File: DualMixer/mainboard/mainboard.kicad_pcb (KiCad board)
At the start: 2 copper layers, 35.6 x 107.9 mm, 62 parts, among them J1 IN_A1, J10 IN_B4, J11 OUTB, J12 Conn_02x05_Odd_Even, J13 Conn_01x03_Male, J2 IN_A2, J3 IN_A3, J4 OUTA, J5 Conn_02x06_Odd_Even, J6 IN_A4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

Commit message: Add missing output connectors to IO board
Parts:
- J5: value Conn_02x06_Odd_Even -> Conn_02x07_Odd_Even; footprint Connector_PinHeader_2.54mm:PinHeader_2x06_P2.54mm_Vertical -> Connector_PinHeader_2.54mm:PinHeader_2x07_P2.54mm_Vertical
- moved J5 23.3 mm to (81.8, 133.4)
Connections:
- J11 pad T: Net-(J11-PadT) -> /OUT_B
- J4 pad T: Net-(J4-PadT) -> /OUT_A
- J5 pad 10: /LEDA -> /LEDB
- J5 pad 11: GND -> /OUT_A
- J5 pad 12: /LEDB -> /OUT_B
- J5 pad 9: GND -> /LEDA
- R20 pad 2: Net-(J11-PadT) -> /OUT_B
- R21 pad 2: Net-(J4-PadT) -> /OUT_A
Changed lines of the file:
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@@
   (net 11 "Net-(J2-PadT)")
   (net 12 "Net-(J3-PadT)")
-  (net 13 "Net-(J4-PadT)")
+  (net 13 "/OUT_A")
   (net 14 "unconnected-(J4-PadTN)")
   (net 15 "/IN_A2")
@@
   (net 26 "Net-(J9-PadT)")
   (net 27 "Net-(J10-PadT)")
-  (net 28 "Net-(J11-PadT)")
+  (net 28 "/OUT_B")
   (net 29 "unconnected-(J11-PadTN)")
   (net 30 "Net-(R1-Pad1)")
@@
   (net 46 "Net-(J12-Pad1)")
   (net 47 "Net-(J12-Pad10)")
+  (net 48 "unconnected-(J5-Pad14)")
   (footprint "Resistor_SMD:R_0603_1608Metric_Pad0.98x0.95mm_HandSolder" (layer "F.Cu")
     (at 156.48 89.2)
@@
       (net 8 "Net-(D3-Pad2)") (pintype "passive"))
     (pad "2" smd roundrect (at 0.9125 0) (size 0.975 0.95) (layers "F.Cu" "F.Paste" "F.Mask") (roundrect_rratio 0.25)
-      (net 28 "Net-(J11-PadT)") (pintype "passive"))
+      (net 28 "/OUT_B") (pintype "passive"))
     (model "${KICAD6_3DMODEL_DIR}/Resistor_SMD.3dshapes/R_0603_1608Metric.wrl"
       (offset (xyz 0 0 0))
@@
       (net 2 "GND") (pintype "passive"))
     (pad "T" thru_hole circle (at 0 11.4 270) (size 2.13 2.13) (drill 1.43) (layers *.Cu *.Mask)
-      (net 28 "Net-(J11-PadT)") (pintype "passive"))
+      (net 28 "/OUT_B") (pintype "passive"))
     (pad "TN" thru_hole circle (at 0 3.1 270) (size 2.13 2.13) (drill 1.42) (layers *.Cu *.Mask)
       (net 29 "unconnected-(J11-PadTN)") (pintype "passive+no_connect"))
@@
       (net 6 "Net-(D1-Pad2)") (pintype "passive"))
     (pad "2" smd roundrect (at 0.9125 0) (size 0.975 0.95) (layers "F.Cu" "F.Paste" "F.Mask") (roundrect_rratio 0.25)
-      (net 13 "Net-(J4-PadT)") (pintype "passive"))
+      (net 13 "/OUT_A") (pintype "passive"))
     (model "${KICAD6_3DMODEL_DIR}/Resistor_SMD.3dshapes/R_0603_1608Metric.wrl"
       (offset (xyz 0 0 0))
@@
       (net 2 "GND") (pintype "passive"))
     (pad "T" thru_hole circle (at 0 11.4 90) (size 2.13 2.13) (drill 1.43) (layers *.Cu *.Mask)
-      (net 13 "Net-(J4-PadT)") (pintype "passive"))
+      (net 13 "/OUT_A") (pintype "passive"))
     (pad "TN" thru_hole circle (at 0 3.1 90) (size 2.13 2.13) (drill 1.42) (layers *.Cu *.Mask)
       (net 14 "unconnected-(J4-PadTN)") (pintype "passive+no_connect"))
@@
     )
   )
-  (footprint "Connector_PinHeader_2.54mm:PinHeader_2x06_P2.54mm_Vertical" (layer "F.Cu")
-    (at 81.87 110.19 180)
-    (descr "Through hole straight pin header, 2x06, 2.54mm pitch, double rows")
-    (tags "Through hole pin header THT 2x06 2.54mm double row")
+  (footprint "Connector_PinHeader_2.54mm:PinHeader_2x07_P2.54mm_Vertical" (layer "F.Cu")
+    (at 81.84 133.44 180)
+    (descr "Through hole straight pin header, 2x07, 2.54mm pitch, double rows")
+    (tags "Through hole pin header THT 2x07 2.54mm double row")
     (property "Sheetfile" "mainboard.kicad_sch")
     (property "Sheetname" "")
     (attr through_hole)
-    (fp_text reference "J5" (at 1.27 -2.33) (layer "F.SilkS")
-      (effects (font (size 1 1) (thickness 0.15)))
-    )
-    (fp_text value "Conn_02x06_Odd_Even" (at 1.27 15.03) (layer "F.Fab")
-      (effects (font (size 1 1) (thickness 0.15)))
-    )
-    (fp_text user "${REFERENCE}" (at 1.27 6.35 90) (layer "F.Fab")
-      (effects (font (size 1 1) (thickness 0.15)))
-    )
-    (fp_line (start -1.33 14.03) (end 3.87 14.03) (layer "F.SilkS") (width 0.12))
+    (fp_text reference "J5" (at 1.35 17.49 180) (layer "F.SilkS")
+      (effects (font (size 1 1) (thickness 0.15)))
+    )
+    (fp_text value "Conn_02x07_Odd_Even" (at 1.27 17.57 180) (layer "F.Fab")
+      (effects (font (size 1 1) (thickness 0.15)))
+    )
+    (fp_text user "${REFERENCE}" (at 1.27 7.62 270) (layer "F.Fab")
+      (effects (font (size 1 1) (thickness 0.15)))
+    )
+    (fp_line (start -1.33 1.27) (end -1.33 16.57) (layer "F.SilkS") (width 0.12))
+    (fp_line (start 3.87 -1.33) (end 3.87 16.57) (layer "F.SilkS") (width 0.12))
+    (fp_line (start -1.33 -1.33) (end 0 -1.33) (layer "F.SilkS") (width 0.12))
+    (fp_line (start -1.33 1.27) (end 1.27 1.27) (layer "F.SilkS") (width 0.12))
+    (fp_line (start -1.33 16.57) (end 3.87 16.57) (layer "F.SilkS") (width 0.12))
+    (fp_line (start 1.27 1.27) (end 1.27 -1.33) (layer "F.SilkS") (width 0.12))
+    (fp_line (start -1.33 0) (end -1.33 -1.33) (layer "F.SilkS") (width 0.12))
     (fp_line (start 1.27 -1.33) (end 3.87 -1.33) (layer "F.SilkS") (width 0.12))
-    (fp_line (start -1.33 1.27) (end 1.27 1.27) (layer "F.SilkS") (width 0.12))
-    (fp_line (start -1.33 1.27) (end -1.33 14.03) (layer "F.SilkS") (width 0.12))
-    (fp_line (start -1.33 0) (end -1.33 -1.33) (layer "F.SilkS") (width 0.12))
-    (fp_line (start -1.33 -1.33) (end 0 -1.33) (layer "F.SilkS") (width 0.12))
-    (fp_line (start 3.87 -1.33) (end 3.87 14.03) (layer "F.SilkS") (width 0.12))
-    (fp_line (start 1.27 1.27) (end 1.27 -1.33) (layer "F.SilkS") (width 0.12))
-    (fp_line (start -1.8 14.5) (end 4.35 14.5) (layer "F.CrtYd") (width 0.05))
-    (fp_line (start -1.8 -1.8) (end -1.8 14.5) (layer "F.CrtYd") (width 0.05))
-    (fp_line (start 4.35 14.5) (end 4.35 -1.8) (layer "F.CrtYd") (width 0.05))
+    (fp_line (start 4.35 17.05) (end 4.35 -1.8) (layer "F.CrtYd") (width 0.05))
     (fp_line (start 4.35 -1.8) (end -1.8 -1.8) (layer "F.CrtYd") (width 0.05))
-    (fp_line (start 3.81 -1.27) (end 3.81 13.97) (layer "F.Fab") (width 0.1))
+    (fp_line (start -1.8 -1.8) (end -1.8 17.05) (layer "F.CrtYd") (width 0.05))
+    (fp_line (start -1.8 17.05) (end 4.35 17.05) (layer "F.CrtYd") (width 0.05))
     (fp_line (start -1.27 0) (end 0 -1.27) (layer "F.Fab") (width 0.1))
-    (fp_line (start -1.27 13.97) (end -1.27 0) (layer "F.Fab") (width 0.1))
-    (fp_line (start 3.81 13.97) (end -1.27 13.97) (layer "F.Fab") (width 0.1))
+    (fp_line (start -1.27 16.51) (end -1.27 0) (layer "F.Fab") (width 0.1))
+    (fp_line (start 3.81 16.51) (end -1.27 16.51) (layer "F.Fab") (width 0.1))
+    (fp_line (start 3.81 -1.27) (end 3.81 16.51) (layer "F.Fab") (width 0.1))
     (fp_line (start 0 -1.27) (end 3.81 -1.27) (layer "F.Fab") (width 0.1))
     (pad "1" thru_hole rect (at 0 0 180) (size 1.7 1.7) (drill 1) (layers *.Cu *.Mask)
@@
       (net 22 "/IN_B3") (pinfunction "Pin_8") (pintype "passive"))
     (pad "9" thru_hole oval (at 0 10.16 180) (size 1.7 1.7) (drill 1) (layers *.Cu *.Mask)
-      (net 2 "GND") (pinfunction "Pin_9") (pintype "passive"))
+      (net 7 "/LEDA") (pinfunction "Pin_9") (pintype "passive"))
     (pad "10" thru_hole oval (at 2.54 10.16 180) (size 1.7 1.7) (drill 1) (layers *.Cu *.Mask)
-      (net 7 "/LEDA") (pinfunction "Pin_10") (pintype "passive"))
+      (net 9 "/LEDB") (pinfunction "Pin_10") (pintype "passive"))
     (pad "11" thru_hole oval (at 0 12.7 180) (size 1.7 1.7) (drill 1) (layers *.Cu *.Mask)
-      (net 2 "GND") (pinfunction "Pin_11") (pintype "passive"))
+      (net 13 "/OUT_A") (pinfunction "Pin_11") (pintype "passive"))
     (pad "12" thru_hole oval (at 2.54 12.7 180) (size 1.7 1.7) (drill 1) (layers *.Cu *.Mask)
-      (net 9 "/LEDB") (pinfunction "Pin_12") (pintype "passive"))
-    (model "${KICAD6_3DMODEL_DIR}/Connector_PinHeader_2.54mm.3dshapes/PinHeader_2x06_P2.54mm_Vertical.wrl"
-      (offset (xyz 0 0 0))
-      (scale (xyz 1 1 1))
+      (net 28 "/OUT_B") (pinfunction "Pin_12") (pintype "passive"))
+    (pad "13" thru_hole oval (at 0 15.24 180) (size 1.7 1.7) (drill 1) (layers *.Cu *.Mask)
+      (net 2 "GND") (pinfunction "Pin_13") (pintype "passive"))
+    (pad "14" thru_hole oval (at 2.54 15.24 180) (size 1.7 1.7) (drill 1) (layers *.Cu *.Mask)
+      (net 48 "unconnected-(J5-Pad14)") (pinfunction "Pin_14") (pintype "passive"))
+    (model "${KICAD6_3DMODEL_DIR}/Connector_PinHeader_2.54mm.3dshapes/PinHeader_2x07_P2.54mm_Vertical.wrl"
+      (offset (xyz 0 0 0))
+      (scale (xyz 1 1 1))

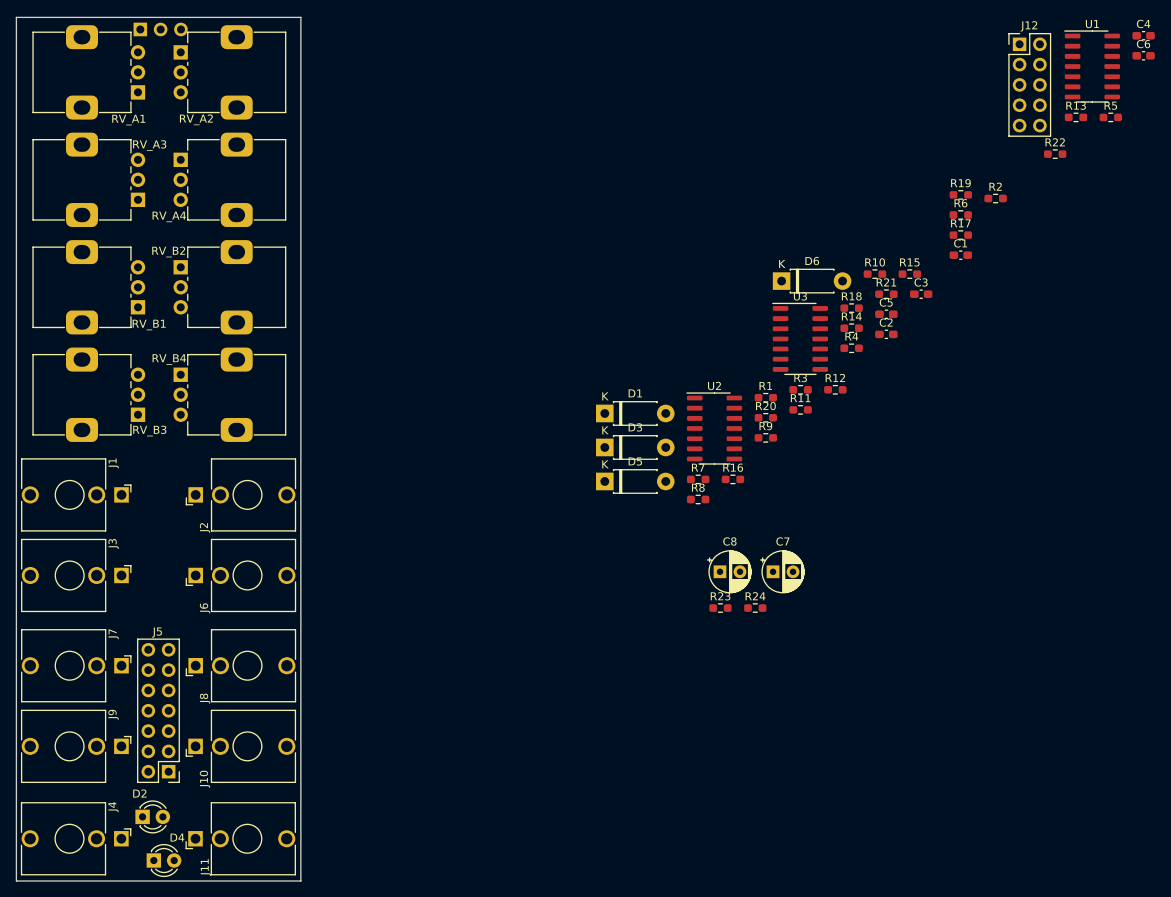
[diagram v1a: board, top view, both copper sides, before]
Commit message: Split up into mainboard and ioboard
And do routing for mainboard
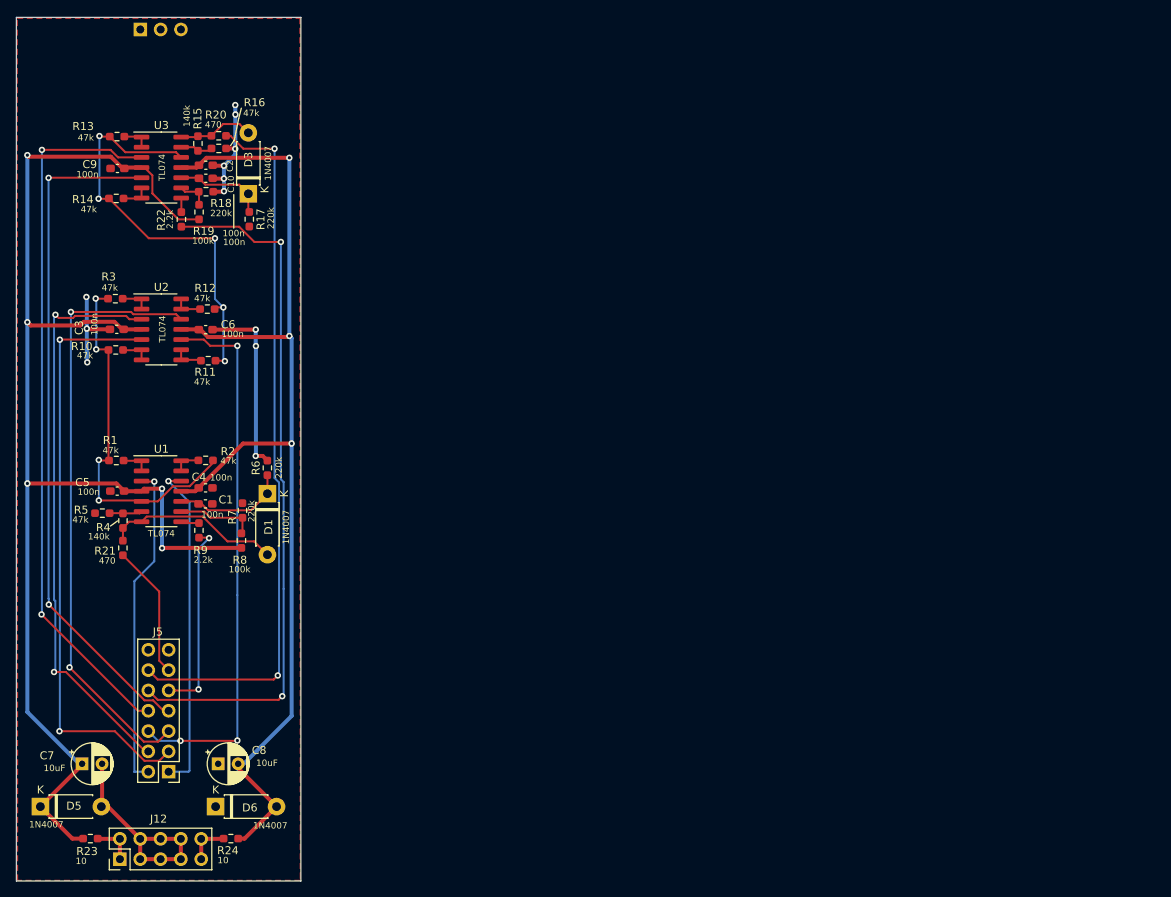
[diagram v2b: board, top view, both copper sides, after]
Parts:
- removed D2: PEAKA, LED_THT:LED_D3.0mm
- removed D4: PEAKB, LED_THT:LED_D3.0mm
- removed J1: IN_A1, Connector_Audio:Jack_3.5mm_QingPu_WQP-PJ398SM_Vertical_CircularHoles
- removed J10: IN_B4, Connector_Audio:Jack_3.5mm_QingPu_WQP-PJ398SM_Vertical_CircularHoles
- removed J11: OUTB, Connector_Audio:Jack_3.5mm_QingPu_WQP-PJ398SM_Vertical_CircularHoles
- removed J2: IN_A2, Connector_Audio:Jack_3.5mm_QingPu_WQP-PJ398SM_Vertical_CircularHoles
- removed J3: IN_A3, Connector_Audio:Jack_3.5mm_QingPu_WQP-PJ398SM_Vertical_CircularHoles
- removed J4: OUTA, Connector_Audio:Jack_3.5mm_QingPu_WQP-PJ398SM_Vertical_CircularHoles
- removed J6: IN_A4, Connector_Audio:Jack_3.5mm_QingPu_WQP-PJ398SM_Vertical_CircularHoles
- removed J7: IN_B1, Connector_Audio:Jack_3.5mm_QingPu_WQP-PJ398SM_Vertical_CircularHoles
- removed J8: IN_B2, Connector_Audio:Jack_3.5mm_QingPu_WQP-PJ398SM_Vertical_CircularHoles
- removed J9: IN_B3, Connector_Audio:Jack_3.5mm_QingPu_WQP-PJ398SM_Vertical_CircularHoles
- removed RV_A1, RV_A2, RV_A3, RV_A4, RV_B1, RV_B2, RV_B3, RV_B4: 100k, Potentiometer_THT:Potentiometer_Alps_RK09K_Single_Vertical
- added C10: 100n, Capacitor_SMD:C_0603_1608Metric_Pad1.08x0.95mm_HandSolder, F.Cu at (86.5, 57.6)
- added C9: 100n, Capacitor_SMD:C_0603_1608Metric_Pad1.08x0.95mm_HandSolder, F.Cu at (75.4, 58.0)
- moved J12 151.7 mm to (75.8, 144.4), turned to 90 degrees
- moved R5 135.4 mm to (73.5, 101.1)
- moved C4 130.2 mm to (86.5, 98.0), turned to 180 degrees
- moved U1 127.9 mm to (80.9, 98.4)
- moved C6 122.1 mm to (86.5, 78.2), turned to 180 degrees
- moved R13 119.9 mm to (75.4, 54.0), turned to 180 degrees
- moved R22 109.5 mm to (83.4, 64.4), turned to -90 degrees
- moved R2 104.0 mm to (86.5, 94.5)
- moved C3 100.6 mm to (75.4, 78.1), turned to 180 degrees
- moved R21 100.6 mm to (76.1, 105.5), turned to -90 degrees
- moved C1 99.4 mm to (86.4, 100.0)
- moved C5 98.7 mm to (75.4, 98.4), turned to 180 degrees
- moved D6 96.5 mm to (87.7, 137.8)
- moved R10 95.4 mm to (75.2, 80.7), turned to 180 degrees
- moved R19 95.2 mm to (85.6, 63.5), turned to 90 degrees
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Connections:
- U3 pad 11: (no net) -> -12V
- U3 pad 4: (no net) -> +12V
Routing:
- net +12V: track 0.00 -> 169.6 mm, vias 0 -> 5
- net -12V: track 0.00 -> 137.4 mm, vias 0 -> 3
- net /OUT_B: track 0.00 -> 89.8 mm, vias 0 -> 2
- net /IN_B3: track 0.00 -> 89.3 mm, vias 0 -> 2
- net /LEDB: track 0.00 -> 87.6 mm, vias 0 -> 2
- net /IN_B4: track 0.00 -> 85.5 mm, vias 0 -> 2
- net GND: track 0.00 -> 78.0 mm, vias 0 -> 12
- net /IN_B2: track 0.00 -> 75.4 mm, vias 0 -> 2
- net /IN_A4: track 0.00 -> 74.9 mm, vias 0 -> 2
- net /IN_A3: track 0.00 -> 72.0 mm, vias 0 -> 2
- net /IN_B1: track 0.00 -> 68.3 mm, vias 0 -> 3
- net Net-(R11-Pad2): track 0.00 -> 54.1 mm, vias 0 -> 5
- net Net-(R1-Pad2): track 0.00 -> 46.3 mm, vias 0 -> 4
- net /IN_A2: track 0.00 -> 41.6 mm, vias 0 -> 1
- net /IN_A1: track 0.00 -> 40.7 mm, vias 0 -> 1
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- added copper zone on F.Cu, net GND

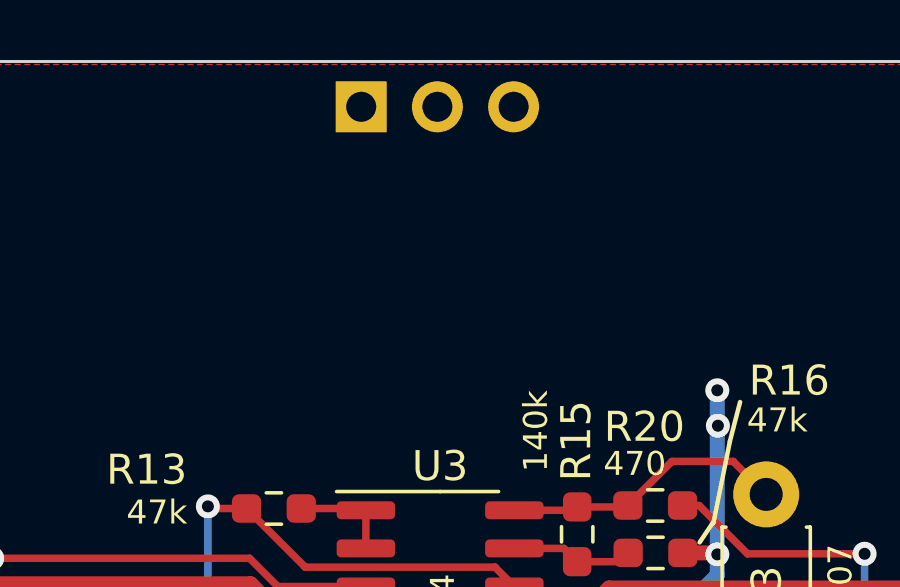
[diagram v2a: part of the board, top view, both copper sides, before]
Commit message: Routed ioboard, add markings to mainboard
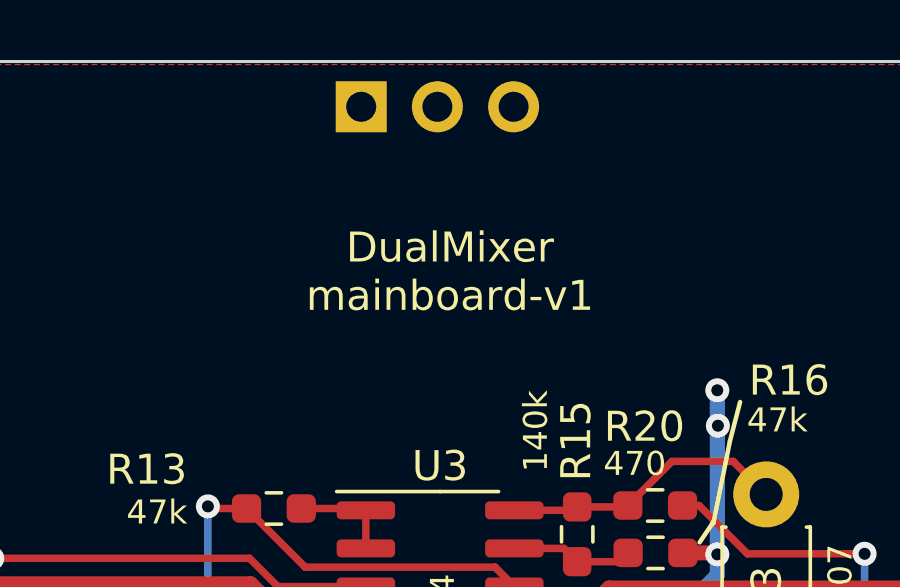
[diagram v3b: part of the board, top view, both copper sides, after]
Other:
- board text added: "DualMixer mainboard-v1"
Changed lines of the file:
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@@
   (gr_line (start 90.93 50.5) (end 90.59 51.81) (layer "F.SilkS") (width 0.15))
   (gr_rect (start 62.81 147.1) (end 98.37 39.15) (layer "Edge.Cuts") (width 0.1) (fill none))
+  (gr_text "DualMixer\nmainboard-v1" (at 81.26 46.16) (layer "F.SilkS")
+    (effects (font (size 1 1) (thickness 0.15)))
+  )
   (segment (start 85.2675 99.65) (end 85.5775 99.96) (width 0.25) (layer "F.Cu") (net 1))
   (segment (start 94.19 98.69) (end 92.12 100.76) (width 0.25) (layer "F.Cu") (net 1))

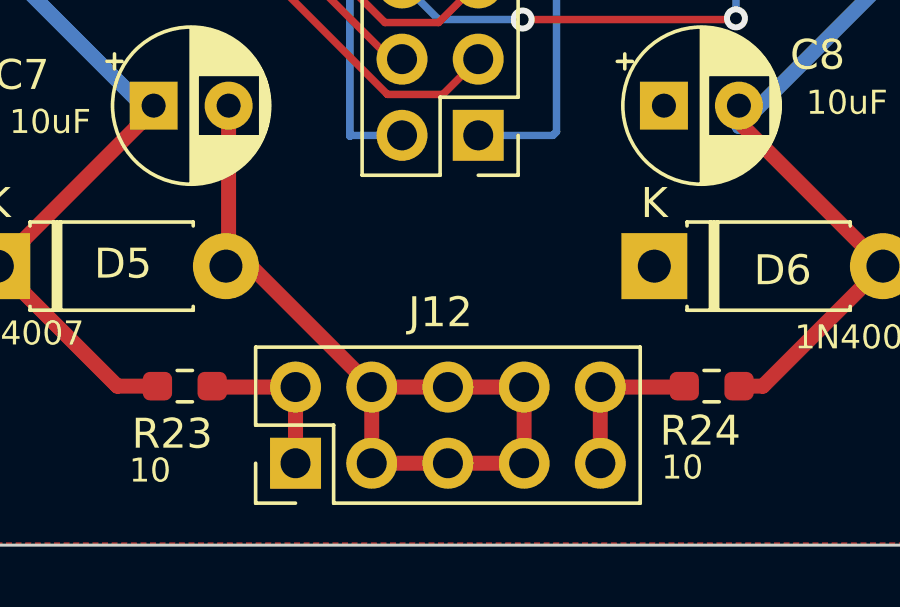
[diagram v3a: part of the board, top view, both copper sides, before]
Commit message: Update power connector graphics
To make it clear how 10-pin IDC connector would be placed w.r.t. +12 and -12.
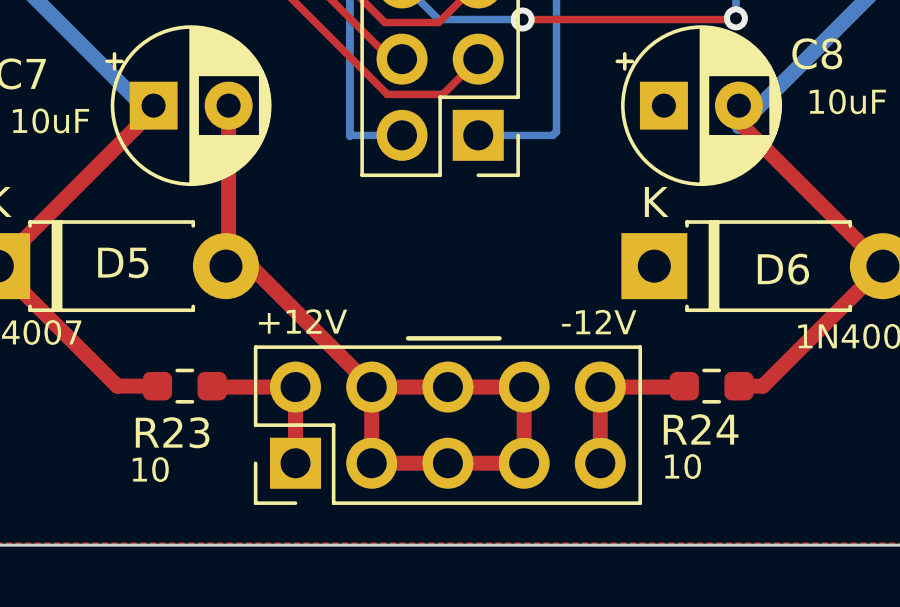
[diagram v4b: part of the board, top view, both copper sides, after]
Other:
- board text added: "+12V"
- board text added: "-12V"
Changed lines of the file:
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@@
     (property "Sheetname" "")
     (attr through_hole)
-    (fp_text reference "J12" (at 5.03 4.83 180) (layer "F.SilkS")
+    (fp_text reference "J12" (at 5.03 4.83 180) (layer "F.Fab")
       (effects (font (size 1 1) (thickness 0.15)))
     )
@@
   (gr_line (start 90.04 54.5) (end 89.58 55.18) (layer "F.SilkS") (width 0.15))
   (gr_line (start 90.93 50.5) (end 90.59 51.81) (layer "F.SilkS") (width 0.15))
+  (gr_line (start 79.502 140.208) (end 82.55 140.208) (layer "F.SilkS") (width 0.15))
   (gr_rect (start 62.81 147.1) (end 98.37 39.15) (layer "Edge.Cuts") (width 0.1) (fill none))
+  (gr_text "+12V" (at 75.946 139.680467) (layer "F.SilkS")
+    (effects (font (size 0.8 0.8) (thickness 0.15)))
+  )
   (gr_text "DualMixer\nmainboard-v1" (at 81.26 46.16) (layer "F.SilkS")
     (effects (font (size 1 1) (thickness 0.15)))
   )
+  (gr_text "-12V" (at 85.852 139.7) (layer "F.SilkS")
+    (effects (font (size 0.8 0.8) (thickness 0.15)))
+  )
   (segment (start 85.2675 99.65) (end 85.5775 99.96) (width 0.25) (layer "F.Cu") (net 1))
